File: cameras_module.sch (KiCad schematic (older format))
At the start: 19 parts, among them J3 WE_68715014522, U3 NTS0102DP, U4 PCA9547BS

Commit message: Added keypads and no flag connections to unused pins
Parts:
- C33: footprint antmicro-footprints:0402-cap -> sc606-baseboard-footprints:0402-cap; symbol antmicroCapacitors0402:C_100n_0402 -> sc606-baseboard:C_100n_0402
- J3: footprint antmicro-footprints:WE_68715014522 -> sc606-baseboard-footprints:WE_68715014522; symbol antmicroFCCConnectors:WE_68715014522 -> sc606-baseboard:WE_68715014522
- R16, R17, R18, R19, R20, R27, R28, R29, R30: footprint antmicro-footprints:0402-res -> sc606-baseboard-footprints:0402-res; symbol antmicroResistors0402:R_2k_0402 -> sc606-baseboard:R_2k_0402
- R21, R22, R23, R24, R25, R26: footprint antmicro-footprints:0402-res -> sc606-baseboard-footprints:0402-res; symbol antmicroResistors0402:R_0R_0402 -> sc606-baseboard:R_0R_0402
- U3: footprint antmicro-footprints:TSSOP-8_W3mm -> sc606-baseboard-footprints:TSSOP-8_W3mm; symbol antmicroLogicTranslatorsLevelShifters:NTS0102DP -> sc606-baseboard:NTS0102DP
- U4: footprint antmicro-footprints:VQFN-24 -> sc606-baseboard-footprints:VQFN-24; symbol antmicroLogicSignalSwitchesMultiplexersDecoders:PCA9547BS -> sc606-baseboard:PCA9547BS
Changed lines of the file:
@@
 Camera I2C multiplexer\n
 $Comp
-L antmicroLogicSignalSwitchesMultiplexersDecoders:PCA9547BS U4
+L sc606-baseboard:PCA9547BS U4
 U 1 1 61E56C5B
 P 4950 4700
 F 0 "U4" H 4850 6089 60  0000 C CNN
 F 1 "PCA9547BS" H 4850 5983 60  0000 C CNN
-F 2 "antmicro-footprints:VQFN-24" H 4700 3300 60  0001 C CNN
+F 2 "sc606-baseboard-footprints:VQFN-24" H 4700 3300 60  0001 C CNN
 F 3 "https://www.nxp.com/docs/en/data-sheet/PCA9547.pdf" H 4950 4700 60  0001 C CNN
 F 4 " NXP" H 4950 4700 50  0001 C CNN "Manufacturer"
@@
 $EndComp
 $Comp
-L antmicroCapacitors0402:C_100n_0402 C33
+L sc606-baseboard:C_100n_0402 C33
 U 1 1 61E589C6
 P 4000 5100
 F 0 "C33" H 4115 5145 60  0000 L CNN
 F 1 "C_100n_0402" H 4000 4950 60  0001 C CNN
-F 2 "antmicro-footprints:0402-cap" H 4200 5300 60  0001 L CNN
+F 2 "sc606-baseboard-footprints:0402-cap" H 4200 5300 60  0001 L CNN
 F 3 "" H 4000 5100 50  0001 C CNN
 F 4 "Walsin" H 4200 5500 60  0001 L CNN "Manufacturer"
@@
 	4000 3600 4000 4950
 $Comp
-L power:GND #PWR042
+L sc606-baseboard:GND #PWR042
 U 1 1 61E5F2B7
 P 4000 6350
@@
 	3250 3900 2050 3900
 $Comp
-L antmicroResistors0402:R_0R_0402 R21
+L sc606-baseboard:R_0R_0402 R21
 U 1 1 61E63E68
 P 3700 3800
 F 0 "R21" H 3700 4013 60  0000 C CNN
 F 1 "R_0R_0402" H 3700 3650 60  0001 C CNN
-F 2 "antmicro-footprints:0402-res" H 3900 4000 60  0001 L CNN
+F 2 "sc606-baseboard-footprints:0402-res" H 3900 4000 60  0001 L CNN
 F 3 "" H 3700 3800 50  0001 C CNN
 F 4 "PANASONIC" H 3900 4200 60  0001 L CNN "Manufacturer"
@@
 	3850 3800 4450 3800
 $Comp
-L antmicroResistors0402:R_0R_0402 R22
+L sc606-baseboard:R_0R_0402 R22
 U 1 1 61E641DF
 P 3700 3900
 F 0 "R22" H 3700 3777 60  0000 C CNN
 F 1 "R_0R_0402" H 3700 3750 60  0001 C CNN
-F 2 "antmicro-footprints:0402-res" H 3900 4100 60  0001 L CNN
+F 2 "sc606-baseboard-footprints:0402-res" H 3900 4100 60  0001 L CNN
 F 3 "" H 3700 3900 50  0001 C CNN
 F 4 "PANASONIC" H 3900 4300 60  0001 L CNN "Manufacturer"
@@
 	2950 3400 3250 3400
 $Comp
-L antmicroResistors0402:R_2k_0402 R19
+L sc606-baseboard:R_2k_0402 R19
 U 1 1 61E68958
 P 2950 3550
 F 0 "R19" V 2905 3620 60  0000 L CNN
 F 1 "R_2k_0402" H 2950 3400 60  0001 C CNN
-F 2 "antmicro-footprints:0402-res" H 3150 3750 60  0001 L CNN
+F 2 "sc606-baseboard-footprints:0402-res" H 3150 3750 60  0001 L CNN
 F 3 "" H 2950 3550 50  0001 C CNN
 F 4 "VISHAY" H 3150 3950 60  0001 L CNN "Manufacturer"
@@
 $EndComp
 $Comp
-L antmicroResistors0402:R_2k_0402 R20
+L sc606-baseboard:R_2k_0402 R20
 U 1 1 61E68DEE
 P 3250 3550
 F 0 "R20" V 3205 3620 60  0000 L CNN
 F 1 "R_2k_0402" H 3250 3400 60  0001 C CNN
-F 2 "antmicro-footprints:0402-res" H 3450 3750 60  0001 L CNN
+F 2 "sc606-baseboard-footprints:0402-res" H 3450 3750 60  0001 L CNN
 F 3 "" H 3250 3550 50  0001 C CNN
 F 4 "VISHAY" H 3450 3950 60  0001 L CNN "Manufacturer"
@@
 	4450 4500 4450 5800
 $Comp
-L antmicroResistors0402:R_0R_0402 R23
+L sc606-baseboard:R_0R_0402 R23
 U 1 1 61E6A5CA
 P 6150 3600
 F 0 "R23" H 6350 3650 60  0000 C CNN
 F 1 "R_0R_0402" H 6150 3450 60  0001 C CNN
-F 2 "antmicro-footprints:0402-res" H 6350 3800 60  0001 L CNN
+F 2 "sc606-baseboard-footprints:0402-res" H 6350 3800 60  0001 L CNN
 F 3 "" H 6150 3600 50  0001 C CNN
 F 4 "PANASONIC" H 6350 4000 60  0001 L CNN "Manufacturer"
@@
 $EndComp
 $Comp
-L antmicroResistors0402:R_0R_0402 R24
+L sc606-baseboard:R_0R_0402 R24
 U 1 1 61E6AAD1
 P 6150 3700
 F 0 "R24" H 6350 3750 60  0000 C CNN
 F 1 "R_0R_0402" H 6150 3550 60  0001 C CNN
-F 2 "antmicro-footprints:0402-res" H 6350 3900 60  0001 L CNN
+F 2 "sc606-baseboard-footprints:0402-res" H 6350 3900 60  0001 L CNN
 F 3 "" H 6150 3700 50  0001 C CNN
 F 4 "PANASONIC" H 6350 4100 60  0001 L CNN "Manufacturer"
@@
 $EndComp
 $Comp
-L antmicroResistors0402:R_0R_0402 R25
+L sc606-baseboard:R_0R_0402 R25
 U 1 1 61E6AE4A
 P 6150 3900
 F 0 "R25" H 6350 3950 60  0000 C CNN
 F 1 "R_0R_0402" H 6150 3750 60  0001 C CNN
-F 2 "antmicro-footprints:0402-res" H 6350 4100 60  0001 L CNN
+F 2 "sc606-baseboard-footprints:0402-res" H 6350 4100 60  0001 L CNN
 F 3 "" H 6150 3900 50  0001 C CNN
 F 4 "PANASONIC" H 6350 4300 60  0001 L CNN "Manufacturer"
@@
 $EndComp
 $Comp
-L antmicroResistors0402:R_0R_0402 R26
+L sc606-baseboard:R_0R_0402 R26
 U 1 1 61E6B0E9
 P 6150 4000
 F 0 "R26" H 6350 4050 60  0000 C CNN
 F 1 "R_0R_0402" H 6150 3850 60  0001 C CNN
-F 2 "antmicro-footprints:0402-res" H 6350 4200 60  0001 L CNN
+F 2 "sc606-baseboard-footprints:0402-res" H 6350 4200 60  0001 L CNN
 F 3 "" H 6150 4000 50  0001 C CNN
 F 4 "PANASONIC" H 6350 4400 60  0001 L CNN "Manufacturer"
@@
 Camera FFC\n\n
 $Comp
-L antmicroFCCConnectors:WE_68715014522 J3
+L sc606-baseboard:WE_68715014522 J3
 U 1 1 61E964B1
 P 12800 3900
 F 0 "J3" H 12880 3092 50  0000 L CNN
 F 1 "WE_68715014522" H 12880 3001 50  0000 L CNN
-F 2 "antmicro-footprints:WE_68715014522" H 12600 350 50  0001 C CNN
+F 2 "sc606-baseboard-footprints:WE_68715014522" H 12600 350 50  0001 C CNN
 F 3 "https://katalog.we-online.de/em/datasheet/6871xx14522.pdf" H 12800 250 50  0001 C CNN
 F 4 "68715014522 " H 13200 3300 60  0001 L CNN "MPN"
@@
 	12600 6400 10900 6400
 $Comp
-L antmicroResistors0402:R_2k_0402 R27
+L sc606-baseboard:R_2k_0402 R27
 U 1 1 61EAFCF7
 P 10300 5450
 F 0 "R27" H 10250 5350 60  0000 L CNN
 F 1 "R_2k_0402" H 10300 5300 60  0001 C CNN
-F 2 "antmicro-footprints:0402-res" H 10500 5650 60  0001 L CNN
+F 2 "sc606-baseboard-footprints:0402-res" H 10500 5650 60  0001 L CNN
 F 3 "" H 10300 5450 50  0001 C CNN
 F 4 "VISHAY" H 10500 5850 60  0001 L CNN "Manufacturer"
@@
 $EndComp
 $Comp
-L antmicroResistors0402:R_2k_0402 R28
+L sc606-baseboard:R_2k_0402 R28
 U 1 1 61EB041B
 P 10500 5450
 F 0 "R28" H 10450 5350 60  0000 L CNN
 F 1 "R_2k_0402" H 10500 5300 60  0001 C CNN
-F 2 "antmicro-footprints:0402-res" H 10700 5650 60  0001 L CNN
+F 2 "sc606-baseboard-footprints:0402-res" H 10700 5650 60  0001 L CNN
 F 3 "" H 10500 5450 50  0001 C CNN
 F 4 "VISHAY" H 10700 5850 60  0001 L CNN "Manufacturer"
@@
 $EndComp
 $Comp
-L antmicroResistors0402:R_2k_0402 R29
+L sc606-baseboard:R_2k_0402 R29
 U 1 1 61EB08C8
 P 10700 5450
 F 0 "R29" H 10650 5350 60  0000 L CNN
 F 1 "R_2k_0402" H 10700 5300 60  0001 C CNN
-F 2 "antmicro-footprints:0402-res" H 10900 5650 60  0001 L CNN
+F 2 "sc606-baseboard-footprints:0402-res" H 10900 5650 60  0001 L CNN
 F 3 "" H 10700 5450 50  0001 C CNN
 F 4 "VISHAY" H 10900 5850 60  0001 L CNN "Manufacturer"
@@
 $EndComp
 $Comp
-L antmicroResistors0402:R_2k_0402 R30
+L sc606-baseboard:R_2k_0402 R30
 U 1 1 61EB0CC5
 P 10900 5450
 F 0 "R30" H 10850 5350 60  0000 L CNN
 F 1 "R_2k_0402" H 10900 5300 60  0001 C CNN
-F 2 "antmicro-footprints:0402-res" H 11100 5650 60  0001 L CNN
+F 2 "sc606-baseboard-footprints:0402-res" H 11100 5650 60  0001 L CNN
 F 3 "" H 10900 5450 50  0001 C CNN
 F 4 "VISHAY" H 11100 5850 60  0001 L CNN "Manufacturer"
@@
 CAM_I2C_SCL_MUX
 $Comp
-L antmicroLogicTranslatorsLevelShifters:NTS0102DP U3
+L sc606-baseboard:NTS0102DP U3
 U 1 1 61EE57DC
 P 3700 8750
 F 0 "U3" H 3700 9265 50  0000 C CNN
 F 1 "NTS0102DP" H 3700 9174 50  0000 C CNN
-F 2 "antmicro-footprints:TSSOP-8_W3mm" H 3600 9250 50  0001 C CNN
+F 2 "sc606-baseboard-footprints:TSSOP-8_W3mm" H 3600 9250 50  0001 C CNN
 F 3 "" H 4350 9500 50  0001 C CNN
 F 4 "NTS0102DP" H 3650 8350 50  0001 C CNN "MPN"
@@
 $EndComp
 $Comp
-L power:GND #PWR043
+L sc606-baseboard:GND #PWR043
 U 1 1 61EE63E6
 P 4100 9000
@@
 	2900 8800 3300 8800
 $Comp
-L antmicroResistors0402:R_2k_0402 R18
+L sc606-baseboard:R_2k_0402 R18
 U 1 1 61FFF734
 P 2900 8250
 F 0 "R18" V 2950 8450 60  0000 R CNN
 F 1 "R_2k_0402" H 2900 8100 60  0001 C CNN
-F 2 "antmicro-footprints:0402-res" H 3100 8450 60  0001 L CNN
+F 2 "sc606-baseboard-footprints:0402-res" H 3100 8450 60  0001 L CNN
 F 3 "" H 2900 8250 50  0001 C CNN
 F 4 "VISHAY" H 3100 8650 60  0001 L CNN "Manufacturer"
@@
 $EndComp
 $Comp
-L antmicroResistors0402:R_2k_0402 R16
+L sc606-baseboard:R_2k_0402 R16
 U 1 1 6200206C
 P 2350 8250
 F 0 "R16" V 2500 8250 60  0000 R CNN
 F 1 "R_2k_0402" H 2350 8100 60  0001 C CNN
-F 2 "antmicro-footprints:0402-res" H 2550 8450 60  0001 L CNN
+F 2 "sc606-baseboard-footprints:0402-res" H 2550 8450 60  0001 L CNN
 F 3 "" H 2350 8250 50  0001 C CNN
 F 4 "VISHAY" H 2550 8650 60  0001 L CNN "Manufacturer"
@@
 $EndComp
 $Comp
-L antmicroResistors0402:R_2k_0402 R17
+L sc606-baseboard:R_2k_0402 R17
 U 1 1 62002978
 P 2500 8250
 F 0 "R17" V 2650 8250 60  0000 R CNN
 F 1 "R_2k_0402" H 2500 8100 60  0001 C CNN
-F 2 "antmicro-footprints:0402-res" H 2700 8450 60  0001 L CNN
+F 2 "sc606-baseboard-footprints:0402-res" H 2700 8450 60  0001 L CNN
 F 3 "" H 2500 8250 50  0001 C CNN
 F 4 "VISHAY" H 2700 8650 60  0001 L CNN "Manufacturer"
@@
 CAM_I2C_SCL
 $Comp
-L power:GND #PWR044
+L sc606-baseboard:GND #PWR044
 U 1 1 6206201E
 P 12500 7450

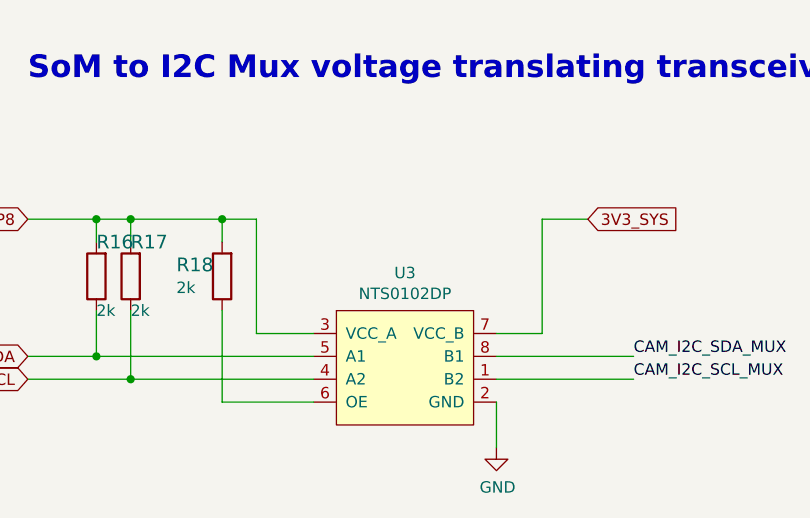
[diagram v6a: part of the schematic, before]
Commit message: LT9611 connected to all needed sources
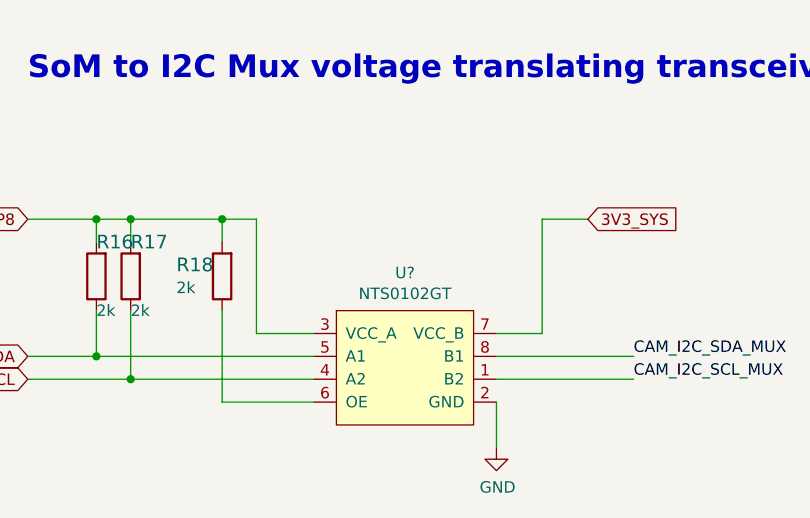
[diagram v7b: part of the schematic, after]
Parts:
- removed U3: NTS0102DP, sc606-baseboard-footprints:TSSOP-8_W3mm, symbol sc606-baseboard:NTS0102DP
- added U?: NTS0102GT, antmicro-footprints:PSON50P100X195X50-8N, symbol antmicroLogicTranslatorsLevelShifters:NTS0102GT
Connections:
- net 3V3_SYS: now also U?.7 (VCC_B)
- net CAM_I2C_SCL: now also U?.4 (A2)
- net CAM_I2C_SCL_MUX: now also U?.1 (B2)
- net CAM_I2C_SDA: now also U?.5 (A1)
- net CAM_I2C_SDA_MUX: now also U?.8 (B1)
- net GND: now also U?.2 (GND)
- net LDO6_1P8: now also U?.3 (VCC_A)
- net at R18.1: now also U?.6 (OE)
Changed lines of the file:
@@
 CAM_I2C_SCL_MUX
-$Comp
-L sc606-baseboard:NTS0102DP U3
-U 1 1 61EE57DC
-P 3700 8750
-F 0 "U3" H 3700 9265 50  0000 C CNN
-F 1 "NTS0102DP" H 3700 9174 50  0000 C CNN
-F 2 "sc606-baseboard-footprints:TSSOP-8_W3mm" H 3600 9250 50  0001 C CNN
-F 3 "" H 4350 9500 50  0001 C CNN
-F 4 "NTS0102DP" H 3650 8350 50  0001 C CNN "MPN"
-F 5 "NXP Semiconductors" H 3800 8450 50  0001 C CNN "Manufacturer"
-	1    3700 8750
-	1    0    0    -1
-$EndComp
 $Comp
 L sc606-baseboard:GND #PWR043
@@
 Wire Bus Line
 	11400 3900 11150 3900
+$Comp
+L antmicroLogicTranslatorsLevelShifters:NTS0102GT U?
+U 1 1 62AE9D15
+P 3700 8750
+F 0 "U?" H 3700 9265 50  0000 C CNN
+F 1 "NTS0102GT" H 3700 9174 50  0000 C CNN
+F 2 "antmicro-footprints:PSON50P100X195X50-8N" H 3600 9250 50  0001 C CNN
+F 3 "http://www.farnell.com/datasheets/1760723.pdf" H 4350 9500 50  0001 C CNN
+F 4 "NTS0102GT" H 3700 9265 50  0001 C CNN "MPN"
+F 5 "NXP Semiconductors" H 3700 9174 50  0001 C CNN "Manufacturer"
+	1    3700 8750
+	1    0    0    -1
+$EndComp
 Wire Bus Line
 	11400 2100 11400 3100

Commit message: Finished connection to HDMI interface. Adjustments after Update of LT9611 symbol
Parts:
- U?: footprint antmicro-footprints:PSON50P100X195X50-8N -> sc606-baseboard-footprints:PSON50P100X195X50-8N; symbol antmicroLogicTranslatorsLevelShifters:NTS0102GT -> sc606-baseboard:NTS0102GT
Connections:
- net CSI_0_CLK_N renamed CSI0_CLK_N
- net CSI_0_CLK_P renamed CSI0_CLK_P
- net CSI_0_LN0_N renamed CSI0_LN0_N
- net CSI_0_LN0_P renamed CSI0_LN0_P
- net CSI_0_LN1_N renamed CSI0_LN1_N
- net CSI_0_LN1_P renamed CSI0_LN1_P
- net CSI_0_LN2_N renamed CSI0_LN2_N
- net CSI_0_LN2_P renamed CSI0_LN2_P
- net CSI_0_LN3_N renamed CSI0_LN3_N
- net CSI_0_LN3_P renamed CSI0_LN3_P
- net CSI_1_CLK_N renamed CSI1_CLK_N
- net CSI_1_CLK_P renamed CSI1_CLK_P
- net CSI_1_LN0_N renamed CSI1_LN0_N
- net CSI_1_LN0_P renamed CSI1_LN0_P
- net CSI_1_LN1_N renamed CSI1_LN1_N
- net CSI_1_LN1_P renamed CSI1_LN1_P
- net CSI_1_LN2_N renamed CSI1_LN2_N
- net CSI_1_LN2_P renamed CSI1_LN2_P
- net CSI_1_LN3_N renamed CSI1_LN3_N
- net CSI_1_LN3_P renamed CSI1_LN3_P
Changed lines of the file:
@@
 	12200 3200 11500 3200
 Text Label 11850 2300 0    50   ~ 0
-CSI_0_LN0_N
+CSI0_LN0_N
 Text Label 11850 2400 0    50   ~ 0
-CSI_0_LN0_P
+CSI0_LN0_P
 Text Label 11850 2500 0    50   ~ 0
-CSI_0_LN1_N
+CSI0_LN1_N
 Text Label 11850 2600 0    50   ~ 0
-CSI_0_LN1_P
+CSI0_LN1_P
 Text Label 11850 2700 0    50   ~ 0
-CSI_0_LN2_N
+CSI0_LN2_N
 Text Label 11850 2800 0    50   ~ 0
-CSI_0_LN2_P
+CSI0_LN2_P
 Text Label 11850 2900 0    50   ~ 0
-CSI_0_LN3_N
+CSI0_LN3_N
 Text Label 11850 3000 0    50   ~ 0
-CSI_0_LN3_P
+CSI0_LN3_P
 Text Label 11750 3100 0    50   ~ 0
-CSI_0_CLK_N
+CSI0_CLK_N
 Text Label 11750 3200 0    50   ~ 0
-CSI_0_CLK_P
+CSI0_CLK_P
 Text GLabel 11150 2100 0    50   Input ~ 0
 CAM1_DATA
@@
 	12200 5000 11500 5000
 Text Label 11850 4100 0    50   ~ 0
-CSI_1_LN0_N
+CSI1_LN0_N
 Text Label 11850 4200 0    50   ~ 0
-CSI_1_LN0_P
+CSI1_LN0_P
 Text Label 11850 4300 0    50   ~ 0
-CSI_1_LN1_N
+CSI1_LN1_N
 Text Label 11850 4400 0    50   ~ 0
-CSI_1_LN1_P
+CSI1_LN1_P
 Text Label 11850 4500 0    50   ~ 0
-CSI_1_LN2_N
+CSI1_LN2_N
 Text Label 11850 4600 0    50   ~ 0
-CSI_1_LN2_P
+CSI1_LN2_P
 Text Label 11850 4700 0    50   ~ 0
-CSI_1_LN3_N
+CSI1_LN3_N
 Text Label 11850 4800 0    50   ~ 0
-CSI_1_LN3_P
+CSI1_LN3_P
 Text Label 11750 4900 0    50   ~ 0
-CSI_1_CLK_N
+CSI1_CLK_N
 Text Label 11750 5000 0    50   ~ 0
-CSI_1_CLK_P
+CSI1_CLK_P
 Text GLabel 11150 3900 0    50   Input ~ 0
 CAM2_DATA
@@
 	11400 3900 11150 3900
 $Comp
-L antmicroLogicTranslatorsLevelShifters:NTS0102GT U?
+L sc606-baseboard:NTS0102GT U?
 U 1 1 62AE9D15
 P 3700 8750
 F 0 "U?" H 3700 9265 50  0000 C CNN
 F 1 "NTS0102GT" H 3700 9174 50  0000 C CNN
-F 2 "antmicro-footprints:PSON50P100X195X50-8N" H 3600 9250 50  0001 C CNN
+F 2 "sc606-baseboard-footprints:PSON50P100X195X50-8N" H 3600 9250 50  0001 C CNN
 F 3 "http://www.farnell.com/datasheets/1760723.pdf" H 4350 9500 50  0001 C CNN
 F 4 "NTS0102GT" H 3700 9265 50  0001 C CNN "MPN"
